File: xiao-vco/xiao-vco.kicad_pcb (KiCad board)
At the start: 2 copper layers, 38 x 100 mm, 54 parts, among them J1 C2M, J2 C2F, J3 Eurorack Power, J4 CV1, J5 V/OCT, J6 OUT, J7 CV2, J8 C1M, J9 C1F, U1 SeeeduinoXIAO, U2 MCP6002-xSN, U3 MCP6002-xSN, U4 TL072, U5 LM1117-5.0, U6 LM4040DBZ-10

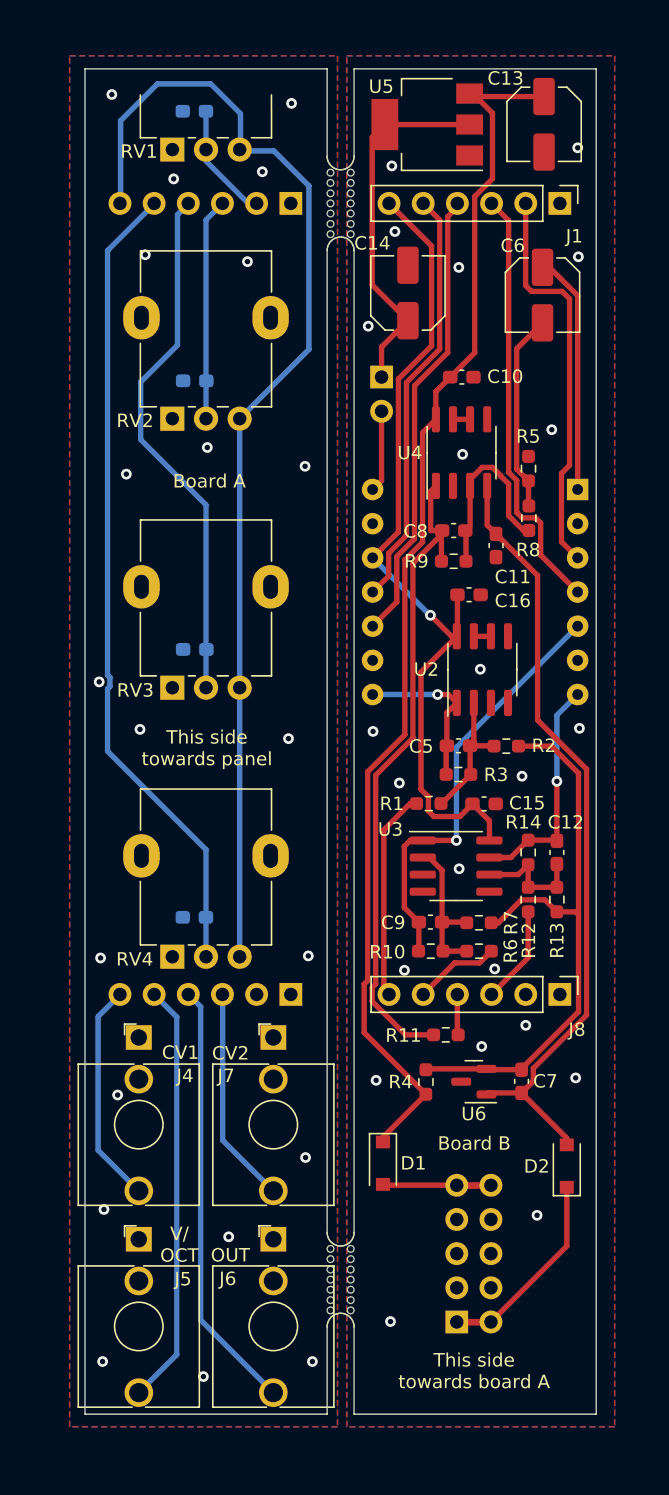
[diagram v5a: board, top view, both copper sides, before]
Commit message: Flip control board for SMD assembly
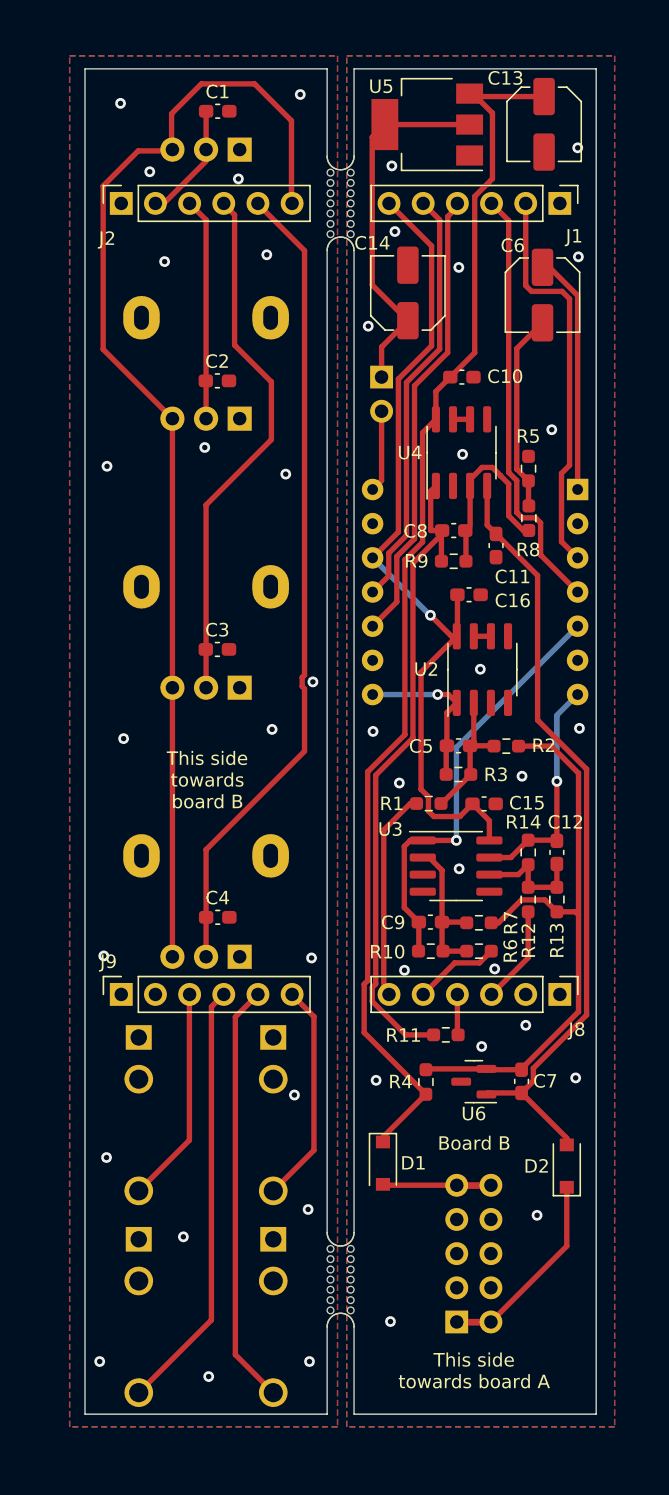
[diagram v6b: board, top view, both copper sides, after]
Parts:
- C1, C2, C3, C4, J2, J9: moved to F.Cu
- J4, J5, J6, J7, RV1, RV2, RV3, RV4: moved to B.Cu
- moved J2 12.6 mm to (152.7, 60.0)
- moved J9 12.6 mm to (152.7, 118.8)
- moved J6 10.0 mm to (154.0, 137.0), turned to 180 degrees
- moved J7 10.0 mm to (154.0, 122.0), turned to 180 degrees
- moved J4 10.00 mm to (164.0, 122.0), turned to 180 degrees
- moved J5 10.00 mm to (164.0, 137.0), turned to 180 degrees
- moved RV1 5.00 mm to (161.5, 56.0)
- moved RV2 5.00 mm to (161.5, 76.0)
- moved RV3 5.00 mm to (161.5, 96.0)
- moved RV4 5.00 mm to (161.5, 116.0)
- moved C4 1.74 mm to (159.9, 113.1), turned to 0 degrees
- moved C1 1.74 mm to (159.9, 53.1), turned to 0 degrees
- moved C2 1.69 mm to (159.8, 73.2), turned to 0 degrees
- moved C3 1.69 mm to (159.8, 93.2), turned to 0 degrees

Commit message: Add LED
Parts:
- added D3: LED, LED_THT:LED_D3.0mm, B.Cu at (160.3, 121.7)
- added R15: 68, Resistor_SMD:R_0603_1608Metric, F.Cu at (159.3, 125.1)
- C1, C10, C11, C12, C15, C16, C2, C3, C4, C5, C7, C8, C9: footprint Capacitor_SMD:C_0603_1608Metric_Pad1.08x0.95mm_HandSolder -> Capacitor_SMD:C_0603_1608Metric
- J4, J5, J6, J7: footprint Connector_Audio:Jack_3.5mm_QingPu_WQP-PJ398SM_Vertical_CircularHoles -> Personal:Thonkiconn
- R1, R10, R11, R12, R13, R14, R2, R3, R4, R5, R6, R7, R8, R9: footprint Resistor_SMD:R_0603_1608Metric_Pad0.98x0.95mm_HandSolder -> Resistor_SMD:R_0603_1608Metric
- RV1: footprint Personal:Potentiometer_Alpha_RD901F-40-00D_Single_Vertical-Hanging -> Personal:Alpha_9mm_Pot_Overhanging
- RV2, RV3, RV4: footprint Potentiometer_THT:Potentiometer_Alpha_RD901F-40-00D_Single_Vertical -> Personal:Alpha_9mm_Pot
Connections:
- J8 pad 2: unconnected-(J8-Pad2) -> /LED
- J9 pad 2: unconnected-(J9-Pad2) -> /CONN_LED
- U1 pad 6: unconnected-(U1-Pad6) -> /LED
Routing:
- net /LED: track 0.00 -> 28.5 mm
- net /CONN_LED: track 0.00 -> 3.88 mm
- net Net-(D3-Pad1): track 0.00 -> 2.99 mm
- net /CONN_OUT: track 32.2 -> 34.1 mm
- net /CONN_VOCT: track 31.5 -> 30.5 mm
- net /CONN_CV2: track 16.1 -> 17.0 mm
- net /POT3_IN: track 32.1 -> 32.7 mm
- net GND1: vias 21 -> 20
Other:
- board text added: "Pots & jacks this side"
- board text added: "This side faces other PCB"
- board text added: "V/OCT"
- board text added: "XDVCO Rev. 1 Paul Battley 2022 CC-BY-SA-4.0"
- board text added: "← Red stripe down"
- board text removed: "Red stripe down"
- board text removed: "This side towards board A"
- board text removed: "This side towards board B"
- board text removed: "This side towards panel"
- board text removed: "V/ OCT"
- board text removed: "Xiao DVCO Rev. 1 Paul Battley 2022 CC-BY-SA-4.0"

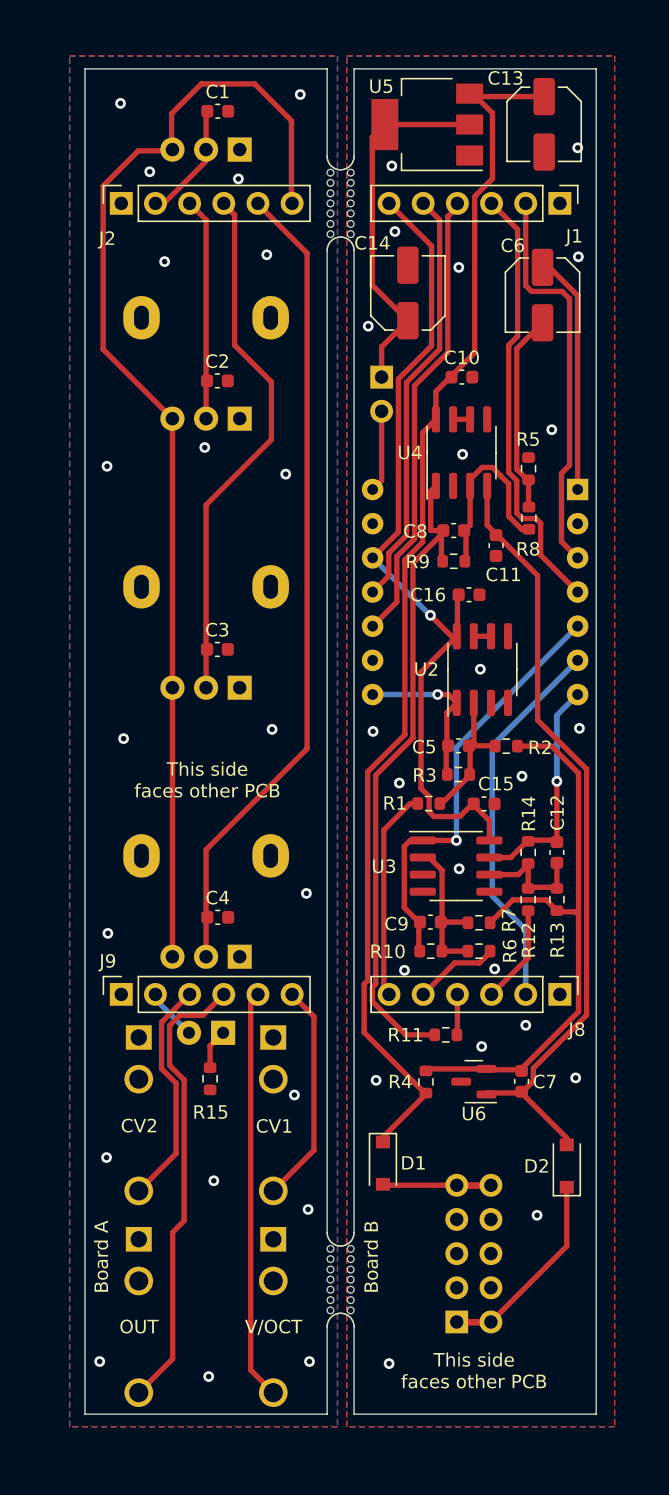
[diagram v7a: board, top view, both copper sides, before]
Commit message: Add switchable 5/8V output
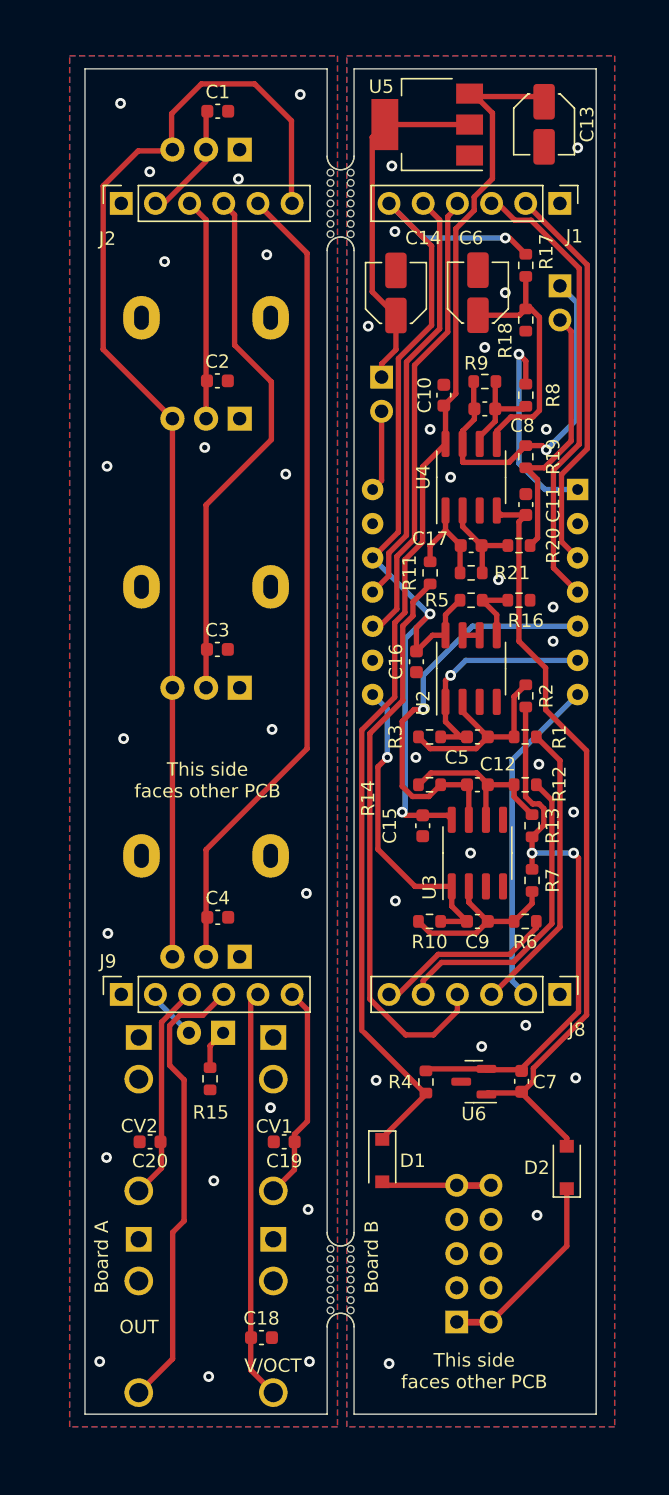
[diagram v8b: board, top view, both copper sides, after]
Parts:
- added C17: 47p, Capacitor_SMD:C_0603_1608Metric, F.Cu at (178.7, 85.4)
- added C18: 1n, Capacitor_SMD:C_0603_1608Metric, F.Cu at (163.1, 144.3)
- added C19: 1n, Capacitor_SMD:C_0603_1608Metric, F.Cu at (164.8, 129.8)
- added C20: 1n, Capacitor_SMD:C_0603_1608Metric, F.Cu at (154.8, 129.8)
- added JP2: Output range, Connector_PinHeader_2.54mm:PinHeader_1x02_P2.54mm_Vertical, B.Cu at (185.3, 66.1)
- added R16: 100k, Resistor_SMD:R_0603_1608Metric, F.Cu at (182.3, 89.5)
- added R17: 330k, Resistor_SMD:R_0603_1608Metric, F.Cu at (182.8, 64.6)
- added R18: 200k, Resistor_SMD:R_0603_1608Metric, F.Cu at (182.8, 68.7)
- added R19: 13k, Resistor_SMD:R_0603_1608Metric, F.Cu at (182.8, 78.8)
- added R20: 20k, Resistor_SMD:R_0603_1608Metric, F.Cu at (182.3, 85.4)
- added R21: 100k, Resistor_SMD:R_0603_1608Metric, F.Cu at (178.7, 87.5)
- C13, C14, C6: footprint Capacitor_SMD:C_Elec_5x5.8 -> Capacitor_SMD:C_Elec_4x5.4
- R10: value 56k -> 100k
- R13: value 200k -> 180k
- R14: value 100k -> 56k
- R5: value 47k -> 100k
- R7: value 180k -> 200k
- R8: value 22k -> 100k
- R9: value 68k -> 100k
- moved R11 34.4 mm to (175.7, 87.5), turned to 90 degrees
- moved R9 13.6 mm to (179.7, 73.2)
- moved R5 10.7 mm to (178.7, 89.5), turned to 0 degrees
- moved C8 9.34 mm to (179.7, 75.3)
- moved R8 9.14 mm to (182.8, 74.3)
- moved R14 8.89 mm to (175.6, 103.2), turned to 0 degrees
- moved R1 8.71 mm to (182.7, 99.7), turned to 180 degrees
- moved R12 8.54 mm to (182.7, 103.2), turned to 180 degrees
- moved C12 7.76 mm to (179.2, 103.2), turned to 180 degrees
- moved C16 6.33 mm to (174.6, 94.1), turned to -90 degrees
- moved R13 5.79 mm to (183.2, 106.3)
- moved R7 5.05 mm to (183.2, 110.3), turned to -90 degrees
- moved C15 4.84 mm to (175.1, 106.3), turned to -90 degrees
- moved C6 4.80 mm to (179.2, 66.6), turned to 90 degrees
- moved R6 4.09 mm to (182.7, 113.4)
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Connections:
- C5 pad 2: /CV1_IN -> /CV2_IN
- C6 pad 1: /AUDIO_OUT -> /VBIAS
- C6 pad 2: Net-(C6-Pad2) -> GND
- C9 pad 2: /CV2_IN -> /CV1_IN
- R1 pad 1: /JACK_CV1 -> /JACK_CV2
- R10 pad 2: /CV2_IN -> /CV1_IN
- R11 pad 2: Net-(C8-Pad1) -> Net-(U4-Pad1)
- R12 pad 1: /JACK_CV2 -> /JACK_VOCT
- R3 pad 2: /CV1_IN -> /CV2_IN
- R5 pad 1: Net-(C6-Pad2) -> +3V3
- R5 pad 2: GND -> Net-(R16-Pad1)
- R6 pad 1: /JACK_VOCT -> /JACK_CV1
- R8 pad 2: Net-(C6-Pad2) -> /AUDIO_OUT
- U1 pad 5: /CV2_IN -> /VOCT_IN
- U1 pad 6: /LED -> /CV2_IN
- U1 pad 7: /VOCT_IN -> /LED
- U2 pad 1: /CV1_IN -> /CV2_IN
- U2 pad 5: GND -> Net-(R16-Pad1)
- U3 pad 1: /CV2_IN -> /CV1_IN
- U4 pad 1: Net-(C8-Pad1) -> Net-(U4-Pad1)
- U4 pad 2: GND -> Net-(C17-Pad2)
- U4 pad 3: Net-(C8-Pad2) -> GND
- U4 pad 5: GND -> /VBIAS
- U4 pad 6: Net-(U4-Pad6) -> Net-(C8-Pad2)
- U4 pad 7: Net-(U4-Pad6) -> Net-(C8-Pad1)
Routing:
- net /JACK_OUT: track 2.95 -> 42.2 mm
- net Net-(C8-Pad1): track 49.3 -> 26.9 mm, vias 0 -> 1
- net Net-(JP2-Pad2): track 0.00 -> 19.9 mm
- net /VBIAS: track 0.00 -> 19.1 mm
- net /JACK_VOCT: track 6.39 -> 23.1 mm
- net /CV2_IN: track 31.9 -> 17.1 mm
- net Net-(C6-Pad2): track 14.8 -> 0.00 mm
- net /JACK_CV2: track 7.27 -> 22.0 mm
- net /VOCT_IN: track 17.1 -> 30.5 mm
- net +3V3: track 62.6 -> 75.6 mm, vias 1 -> 3
- net /CV1_IN: track 12.2 -> 23.9 mm
- net Net-(U4-Pad1): track 0.00 -> 7.94 mm
- net Net-(C17-Pad2): track 0.00 -> 7.20 mm
- net Net-(C8-Pad2): track 13.7 -> 7.49 mm
- net Net-(C5-Pad1): track 10.3 -> 15.5 mm
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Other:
- board text added: "JOAT Rev. 1 Paul Battley 2022 CC-BY-SA-4.0"
- board text added: "µC 5V supply → Remove before plugging USB!"
- board text added: "← With: ±8V Without: ±5V"
- board text removed: "Module 5V supply jumper. Remove before plugging USB!"
- board text removed: "XDVCO Rev. 1 Paul Battley 2022 CC-BY-SA-4.0"
